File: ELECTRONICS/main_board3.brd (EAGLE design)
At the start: 58 x 56 mm, 18 parts, among them CON3 Accelerometer connector, CON4 UART connector, IC1 LM324D, IC2 7414N

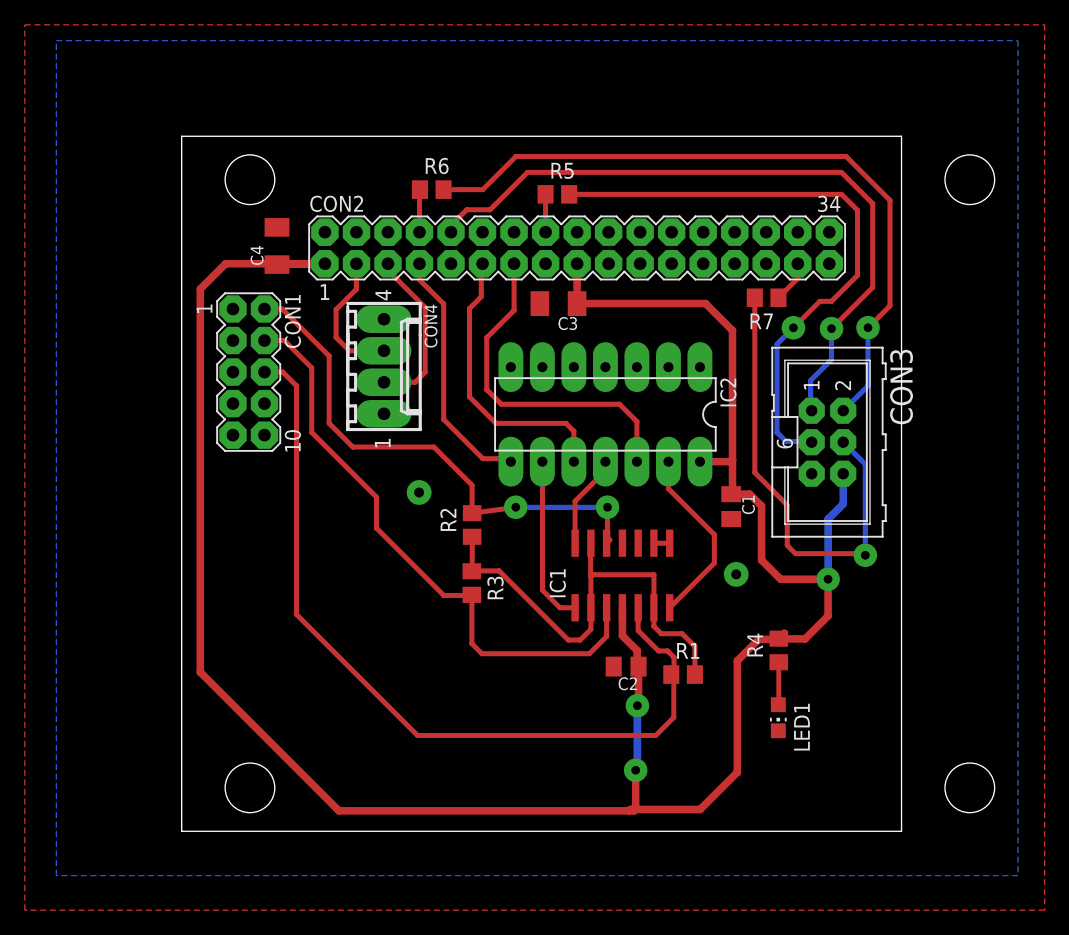
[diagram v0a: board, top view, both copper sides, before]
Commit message: PCB is finished for both boards
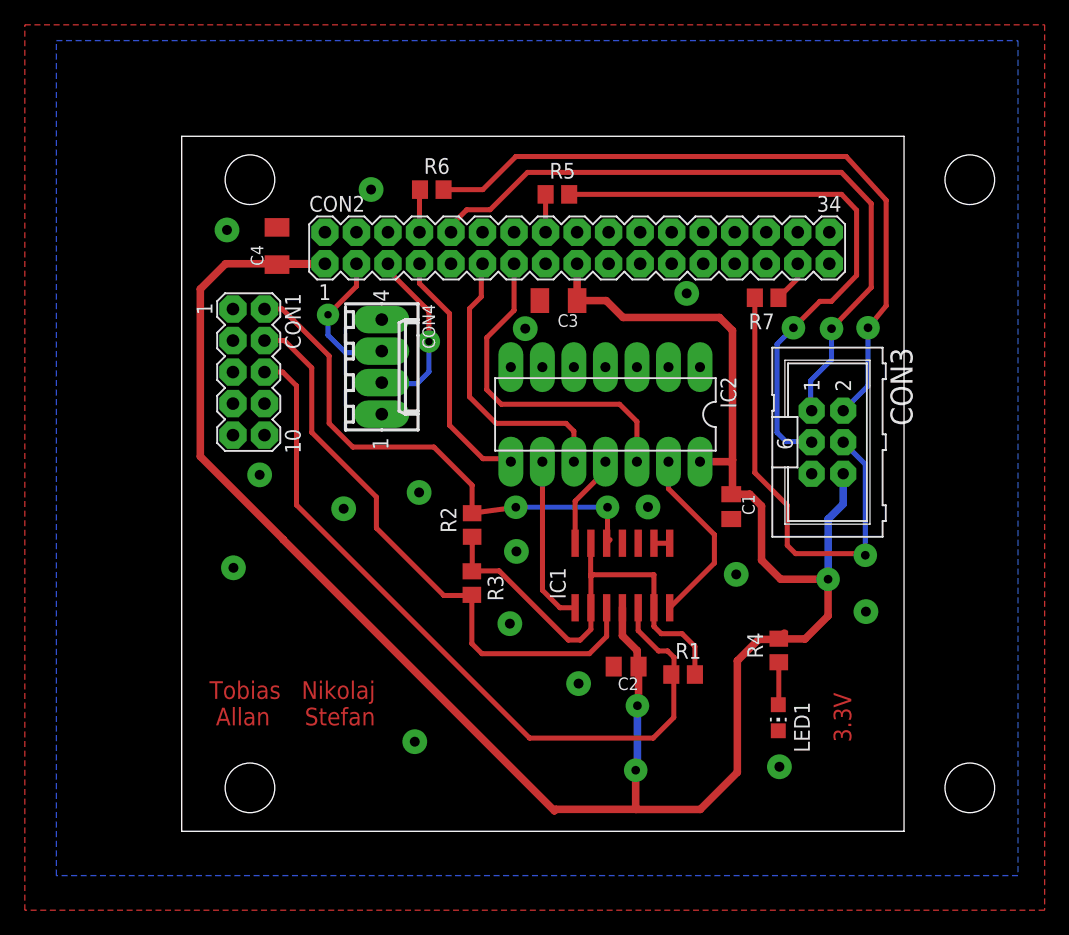
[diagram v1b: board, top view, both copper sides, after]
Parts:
- moved C3 0.24 mm to (30.4, 42.8)
- moved CON4 0.18 mm to (16.1, 37.4)
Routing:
- net +3V3: track 188.4 -> 177.5 mm
- net VFB_C: track 67.2 -> 62.2 mm
- net UART_RX: track 10.9 -> 11.8 mm, vias 0 -> 1
- net UART_TX: track 13.6 -> 14.3 mm, vias 0 -> 1
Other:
- board size 58 x 56 mm -> 58.2 x 56 mm
- board text added: "3.3V"
- board text added: "Tobias Nikolaj Allan Stefan"

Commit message: Final PCB
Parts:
- R1, R2, R3: value 100K -> 10K
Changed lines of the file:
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@@
 <element name="IC2" library="74xx-eu" package="DIL14" value="7414N" x="34.14" y="33.59" rot="R180"/>
 <element name="LED1" library="led" package="CHIP-LED0805" value="Power indicator" x="48.07" y="9.15" rot="R180"/>
-<element name="R1" library="rcl" package="R0805" value="100K" x="40.4" y="12.63"/>
-<element name="R2" library="rcl" package="R0805" value="100K" x="23.4" y="24.68" rot="R90"/>
-<element name="R3" library="rcl" package="R0805" value="100K" x="23.38" y="20" rot="R270"/>
+<element name="R1" library="rcl" package="R0805" value="10K" x="40.4" y="12.63"/>
+<element name="R2" library="rcl" package="R0805" value="10K" x="23.4" y="24.68" rot="R90"/>
+<element name="R3" library="rcl" package="R0805" value="10K" x="23.38" y="20" rot="R270"/>
 <element name="R4" library="rcl" package="R0805" value="100R" x="48.11" y="14.57" rot="R90"/>
 <element name="R5" library="rcl" package="R0805" value="50R" x="30.27" y="51.32"/>
